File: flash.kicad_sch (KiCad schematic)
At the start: 0 parts

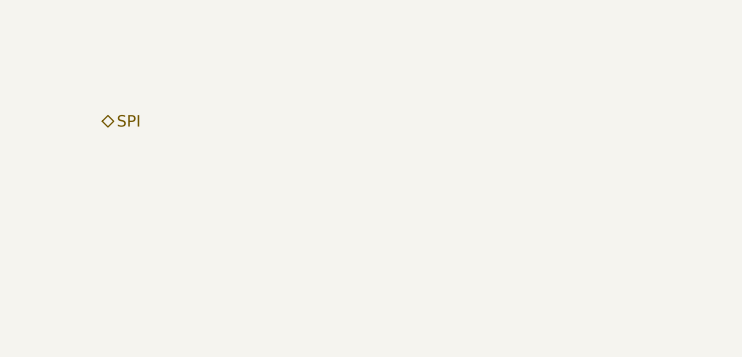
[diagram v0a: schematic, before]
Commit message: Added flash
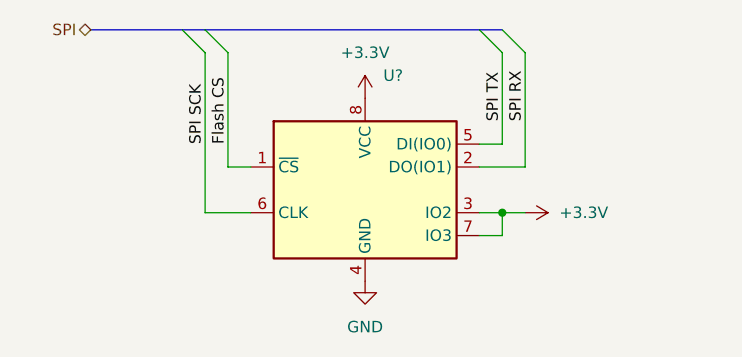
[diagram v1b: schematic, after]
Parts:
- added U?: ~, Package_SO:SOIC-8_5.23x5.23mm_P1.27mm, symbol Memory_Flash:W25Q32JVSS
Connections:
- new net +3V3: U?.3 (IO2), U?.7 (IO3), U?.8 (VCC)
- new net Flash CS: U?.1 (~{CS})
- new net GND: U?.4 (GND)
- new net SPI RX: U?.2 (DO(IO1))
- new net SPI SCK: U?.6 (CLK)
- new net SPI TX: U?.5 (DI(IO0))
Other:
- title: (none) -> Phoenix Flash
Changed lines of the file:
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@@
 (kicad_sch (version 20211123) (generator eeschema)
-  (paper "A4")
-  (hierarchical_label "SPI" (shape bidirectional) (at 25.4 31.75 0)
-    (effects (font (size 1.27 1.27)) (justify left))
+  (paper "A5")
+  (title_block
+    (title "Phoenix Flash")
+    (comment 1 "2022/10/19 WH")
+  )
+  (junction (at 69.85 41.91) (diameter 0) (color 0 0 0 0)
+  )
+  (bus_entry (at 36.83 21.59) (size 2.54 2.54)
+    (stroke (width 0) (type default) (color 0 0 0 0))
+  )
+  (bus_entry (at 34.29 21.59) (size 2.54 2.54)
+    (stroke (width 0) (type default) (color 0 0 0 0))
+  )
+  (bus_entry (at 67.31 21.59) (size 2.54 2.54)
+    (stroke (width 0) (type default) (color 0 0 0 0))
+  )
+  (bus_entry (at 69.85 21.59) (size 2.54 2.54)
+    (stroke (width 0) (type default) (color 0 0 0 0))
+  )
+  (bus (pts (xy 36.83 21.59) (xy 67.31 21.59))
+    (stroke (width 0) (type default) (color 0 0 0 0))
+  )
+  (wire (pts (xy 39.37 24.13) (xy 39.37 36.83))
+    (stroke (width 0) (type default) (color 0 0 0 0))
+  )
+  (wire (pts (xy 39.37 36.83) (xy 41.91 36.83))
+    (stroke (width 0) (type default) (color 0 0 0 0))
+  )
+  (wire (pts (xy 69.85 34.29) (xy 69.85 24.13))
+    (stroke (width 0) (type default) (color 0 0 0 0))
+  )
+  (wire (pts (xy 69.85 41.91) (xy 67.31 41.91))
+    (stroke (width 0) (type default) (color 0 0 0 0))
+  )
+  (wire (pts (xy 36.83 24.13) (xy 36.83 41.91))
+    (stroke (width 0) (type default) (color 0 0 0 0))
+  )
+  (bus (pts (xy 34.29 21.59) (xy 36.83 21.59))
+    (stroke (width 0) (type default) (color 0 0 0 0))
+  )
+  (wire (pts (xy 36.83 41.91) (xy 41.91 41.91))
+    (stroke (width 0) (type default) (color 0 0 0 0))
+  )
+  (bus (pts (xy 67.31 21.59) (xy 69.85 21.59))
+    (stroke (width 0) (type default) (color 0 0 0 0))
+  )
+  (wire (pts (xy 67.31 44.45) (xy 69.85 44.45))
+    (stroke (width 0) (type default) (color 0 0 0 0))
+  )
+  (wire (pts (xy 69.85 44.45) (xy 69.85 41.91))
+    (stroke (width 0) (type default) (color 0 0 0 0))
+  )
+  (wire (pts (xy 69.85 41.91) (xy 72.39 41.91))
+    (stroke (width 0) (type default) (color 0 0 0 0))
+  )
+  (wire (pts (xy 72.39 24.13) (xy 72.39 36.83))
+    (stroke (width 0) (type default) (color 0 0 0 0))
+  )
+  (wire (pts (xy 72.39 36.83) (xy 67.31 36.83))
+    (stroke (width 0) (type default) (color 0 0 0 0))
+  )
+  (wire (pts (xy 67.31 34.29) (xy 69.85 34.29))
+    (stroke (width 0) (type default) (color 0 0 0 0))
+  )
+  (bus (pts (xy 24.13 21.59) (xy 34.29 21.59))
+    (stroke (width 0) (type default) (color 0 0 0 0))
+  )
+  (label "SPI SCK" (at 36.83 34.29 90)
+    (effects (font (size 1.27 1.27)) (justify left bottom))
+  )
+  (label "SPI RX" (at 72.39 31.75 90)
+    (effects (font (size 1.27 1.27)) (justify left bottom))
+  )
+  (label "Flash CS" (at 39.37 34.29 90)
+    (effects (font (size 1.27 1.27)) (justify left bottom))
+  )
+  (label "SPI TX" (at 69.85 31.75 90)
+    (effects (font (size 1.27 1.27)) (justify left bottom))
+  )
+  (hierarchical_label "SPI" (shape bidirectional) (at 24.13 21.59 180)
+    (effects (font (size 1.27 1.27)) (justify right))
+  )
+  (symbol (lib_id "power:+3.3V") (at 72.39 41.91 270) (unit 1)
+    (in_bom yes) (on_board yes) (fields_autoplaced)
+    (property "Reference" "#PWR?" (id 0) (at 68.58 41.91 0)
+      (effects (font (size 1.27 1.27)) hide)
+    )
+    (property "Value" "+3.3V" (id 1) (at 76.2 41.9099 90)
+      (effects (font (size 1.27 1.27)) (justify left))
+    )
+    (property "Footprint" "" (id 2) (at 72.39 41.91 0)
+      (effects (font (size 1.27 1.27)) hide)
+    )
+    (property "Datasheet" "" (id 3) (at 72.39 41.91 0)
+      (effects (font (size 1.27 1.27)) hide)
+    )
+    (pin "1")
+  )
+  (symbol (lib_id "power:GND") (at 54.61 49.53 0) (unit 1)
+    (in_bom yes) (on_board yes) (fields_autoplaced)
+    (property "Reference" "#PWR?" (id 0) (at 54.61 55.88 0)
+      (effects (font (size 1.27 1.27)) hide)
+    )
+    (property "Value" "GND" (id 1) (at 54.61 54.61 0))
+    (property "Footprint" "" (id 2) (at 54.61 49.53 0)
+      (effects (font (size 1.27 1.27)) hide)
+    )
+    (property "Datasheet" "" (id 3) (at 54.61 49.53 0)
+      (effects (font (size 1.27 1.27)) hide)
+    )
+    (pin "1")
+  )
+  (symbol (lib_id "Memory_Flash:W25Q32JVSS") (at 54.61 39.37 0) (unit 1)
+    (in_bom yes) (on_board yes) (fields_autoplaced)
+    (property "Reference" "U?" (id 0) (at 56.6294 26.67 0)
+      (effects (font (size 1.27 1.27)) (justify left))
+    )
+    (property "Value" "~" (id 1) (at 56.6294 29.21 0)
+      (effects (font (size 1.27 1.27)) (justify left))
+    )
+    (property "Footprint" "Package_SO:SOIC-8_5.23x5.23mm_P1.27mm" (id 2) (at 54.61 39.37 0)
+      (effects (font (size 1.27 1.27)) hide)
+    )
+    (property "Datasheet" "http://www.winbond.com/resource-files/w25q32jv%20revg%2003272018%20plus.pdf" (id 3) (at 54.61 39.37 0)
+      (effects (font (size 1.27 1.27)) hide)
+    )
+    (property "JLC" "SOP-8_5.2x5.3x1.27P" (id 4) (at 54.61 39.37 0)
+      (effects (font (size 1.27 1.27)) hide)
+    )
+    (property "LCSC" "C83140" (id 5) (at 54.61 39.37 0)
+      (effects (font (size 1.27 1.27)) hide)
+    )
+    (pin "1")
+    (pin "2")
+    (pin "3")
+    (pin "4")
+    (pin "5")
+    (pin "6")
+    (pin "7")
+    (pin "8")
+  )
+  (symbol (lib_id "power:+3.3V") (at 54.61 29.21 0) (unit 1)
+    (in_bom yes) (on_board yes) (fields_autoplaced)
+    (property "Reference" "#PWR?" (id 0) (at 54.61 33.02 0)
+      (effects (font (size 1.27 1.27)) hide)
+    )
+    (property "Value" "+3.3V" (id 1) (at 54.61 24.13 0))
+    (property "Footprint" "" (id 2) (at 54.61 29.21 0)
+      (effects (font (size 1.27 1.27)) hide)
+    )
+    (property "Datasheet" "" (id 3) (at 54.61 29.21 0)
+      (effects (font (size 1.27 1.27)) hide)
+    )
+    (pin "1")
   )
 )

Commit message: Added decoupling cap to flash
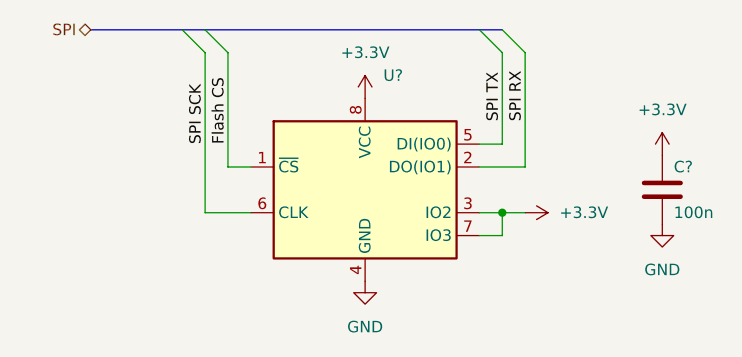
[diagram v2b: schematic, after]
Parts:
- added C?: 100n, Capacitor_SMD:C_0603_1608Metric, symbol Device:C
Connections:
- net +3V3: now also C?.1
- net GND: now also C?.2
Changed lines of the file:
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@@
     (pin "1")
+  )
+  (symbol (lib_id "power:+3.3V") (at 87.63 35.56 0) (unit 1)
+    (in_bom yes) (on_board yes) (fields_autoplaced)
+    (property "Reference" "#PWR?" (id 0) (at 87.63 39.37 0)
+      (effects (font (size 1.27 1.27)) hide)
+    )
+    (property "Value" "+3.3V" (id 1) (at 87.63 30.48 0))
+    (property "Footprint" "" (id 2) (at 87.63 35.56 0)
+      (effects (font (size 1.27 1.27)) hide)
+    )
+    (property "Datasheet" "" (id 3) (at 87.63 35.56 0)
+      (effects (font (size 1.27 1.27)) hide)
+    )
+    (pin "1")
+  )
+  (symbol (lib_id "Device:C") (at 87.63 39.37 0) (unit 1)
+    (in_bom yes) (on_board yes)
+    (property "Reference" "C?" (id 0) (at 88.9 36.83 0)
+      (effects (font (size 1.27 1.27)) (justify left))
+    )
+    (property "Value" "100n" (id 1) (at 88.9 41.91 0)
+      (effects (font (size 1.27 1.27)) (justify left))
+    )
+    (property "Footprint" "Capacitor_SMD:C_0603_1608Metric" (id 2) (at 88.5952 43.18 0)
+      (effects (font (size 1.27 1.27)) hide)
+    )
+    (property "Datasheet" "~" (id 3) (at 87.63 39.37 0)
+      (effects (font (size 1.27 1.27)) hide)
+    )
+    (property "LCSC" "C14663" (id 4) (at 87.63 39.37 0)
+      (effects (font (size 1.27 1.27)) hide)
+    )
+    (property "JLC" "0603" (id 5) (at 87.63 39.37 0)
+      (effects (font (size 1.27 1.27)) hide)
+    )
+    (pin "1")
+    (pin "2")
   )
   (symbol (lib_id "Memory_Flash:W25Q32JVSS") (at 54.61 39.37 0) (unit 1)
@@
     (pin "8")
   )
+  (symbol (lib_id "power:GND") (at 87.63 43.18 0) (unit 1)
+    (in_bom yes) (on_board yes) (fields_autoplaced)
+    (property "Reference" "#PWR?" (id 0) (at 87.63 49.53 0)
+      (effects (font (size 1.27 1.27)) hide)
+    )
+    (property "Value" "GND" (id 1) (at 87.63 48.26 0))
+    (property "Footprint" "" (id 2) (at 87.63 43.18 0)
+      (effects (font (size 1.27 1.27)) hide)
+    )
+    (property "Datasheet" "" (id 3) (at 87.63 43.18 0)
+      (effects (font (size 1.27 1.27)) hide)
+    )
+    (pin "1")
+  )
   (symbol (lib_id "power:+3.3V") (at 54.61 29.21 0) (unit 1)

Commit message: Fixed bus names
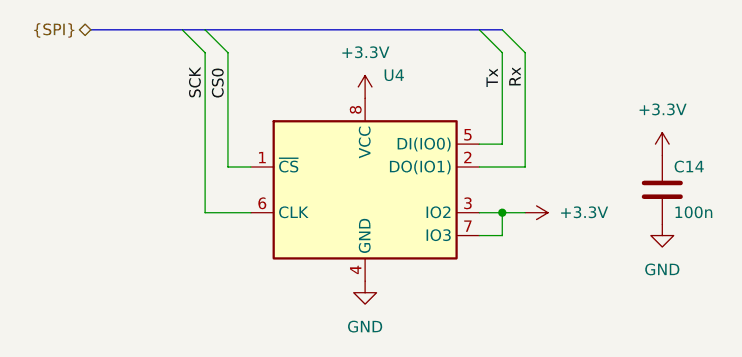
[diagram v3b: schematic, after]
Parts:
- gave numbers to parts that had none: 2
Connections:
- net Flash CS renamed CS0
- net SPI RX renamed Rx
- net SPI SCK renamed SCK
- net SPI TX renamed Tx
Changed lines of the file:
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@@
     (stroke (width 0) (type default) (color 0 0 0 0))
   )
-  (label "SPI SCK" (at 36.83 34.29 90)
+  (label "SCK" (at 36.83 29.21 90)
     (effects (font (size 1.27 1.27)) (justify left bottom))
   )
-  (label "SPI RX" (at 72.39 31.75 90)
+  (label "Rx" (at 72.39 27.94 90)
     (effects (font (size 1.27 1.27)) (justify left bottom))
   )
-  (label "Flash CS" (at 39.37 34.29 90)
+  (label "CS0" (at 39.37 29.21 90)
     (effects (font (size 1.27 1.27)) (justify left bottom))
   )
-  (label "SPI TX" (at 69.85 31.75 90)
+  (label "Tx" (at 69.85 27.94 90)
     (effects (font (size 1.27 1.27)) (justify left bottom))
   )
-  (hierarchical_label "SPI" (shape bidirectional) (at 24.13 21.59 180)
+  (hierarchical_label "{SPI}" (shape bidirectional) (at 24.13 21.59 180)
     (effects (font (size 1.27 1.27)) (justify right))
   )
   (symbol (lib_id "power:+3.3V") (at 72.39 41.91 270) (unit 1)
     (in_bom yes) (on_board yes) (fields_autoplaced)
-    (property "Reference" "#PWR?" (id 0) (at 68.58 41.91 0)
+    (property "Reference" "#PWR0130" (id 0) (at 68.58 41.91 0)
       (effects (font (size 1.27 1.27)) hide)
     )
@@
   (symbol (lib_id "power:GND") (at 54.61 49.53 0) (unit 1)
     (in_bom yes) (on_board yes) (fields_autoplaced)
-    (property "Reference" "#PWR?" (id 0) (at 54.61 55.88 0)
+    (property "Reference" "#PWR0129" (id 0) (at 54.61 55.88 0)
       (effects (font (size 1.27 1.27)) hide)
     )
@@
   (symbol (lib_id "power:+3.3V") (at 87.63 35.56 0) (unit 1)
     (in_bom yes) (on_board yes) (fields_autoplaced)
-    (property "Reference" "#PWR?" (id 0) (at 87.63 39.37 0)
+    (property "Reference" "#PWR0131" (id 0) (at 87.63 39.37 0)
       (effects (font (size 1.27 1.27)) hide)
     )
@@
   (symbol (lib_id "Device:C") (at 87.63 39.37 0) (unit 1)
     (in_bom yes) (on_board yes)
-    (property "Reference" "C?" (id 0) (at 88.9 36.83 0)
+    (property "Reference" "C14" (id 0) (at 88.9 36.83 0)
       (effects (font (size 1.27 1.27)) (justify left))
     )
@@
   (symbol (lib_id "Memory_Flash:W25Q32JVSS") (at 54.61 39.37 0) (unit 1)
     (in_bom yes) (on_board yes) (fields_autoplaced)
-    (property "Reference" "U?" (id 0) (at 56.6294 26.67 0)
+    (property "Reference" "U4" (id 0) (at 56.6294 26.67 0)
       (effects (font (size 1.27 1.27)) (justify left))
     )
@@
   (symbol (lib_id "power:GND") (at 87.63 43.18 0) (unit 1)
     (in_bom yes) (on_board yes) (fields_autoplaced)
-    (property "Reference" "#PWR?" (id 0) (at 87.63 49.53 0)
+    (property "Reference" "#PWR0133" (id 0) (at 87.63 49.53 0)
       (effects (font (size 1.27 1.27)) hide)
     )
@@
   (symbol (lib_id "power:+3.3V") (at 54.61 29.21 0) (unit 1)
     (in_bom yes) (on_board yes) (fields_autoplaced)
-    (property "Reference" "#PWR?" (id 0) (at 54.61 33.02 0)
+    (property "Reference" "#PWR0128" (id 0) (at 54.61 33.02 0)
       (effects (font (size 1.27 1.27)) hide)
     )

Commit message: Various updates because I forgot to commit for a while
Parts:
- renumbered C14 to C19, U4 to U7
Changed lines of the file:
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@@
   (symbol (lib_id "power:+3.3V") (at 72.39 41.91 270) (unit 1)
     (in_bom yes) (on_board yes) (fields_autoplaced)
-    (property "Reference" "#PWR0130" (id 0) (at 68.58 41.91 0)
+    (property "Reference" "#PWR040" (id 0) (at 68.58 41.91 0)
       (effects (font (size 1.27 1.27)) hide)
     )
@@
   (symbol (lib_id "power:GND") (at 54.61 49.53 0) (unit 1)
     (in_bom yes) (on_board yes) (fields_autoplaced)
-    (property "Reference" "#PWR0129" (id 0) (at 54.61 55.88 0)
+    (property "Reference" "#PWR039" (id 0) (at 54.61 55.88 0)
       (effects (font (size 1.27 1.27)) hide)
     )
@@
   (symbol (lib_id "power:+3.3V") (at 87.63 35.56 0) (unit 1)
     (in_bom yes) (on_board yes) (fields_autoplaced)
-    (property "Reference" "#PWR0131" (id 0) (at 87.63 39.37 0)
+    (property "Reference" "#PWR041" (id 0) (at 87.63 39.37 0)
       (effects (font (size 1.27 1.27)) hide)
     )
@@
   (symbol (lib_id "Device:C") (at 87.63 39.37 0) (unit 1)
     (in_bom yes) (on_board yes)
-    (property "Reference" "C14" (id 0) (at 88.9 36.83 0)
+    (property "Reference" "C19" (id 0) (at 88.9 36.83 0)
       (effects (font (size 1.27 1.27)) (justify left))
     )
@@
   (symbol (lib_id "Memory_Flash:W25Q32JVSS") (at 54.61 39.37 0) (unit 1)
     (in_bom yes) (on_board yes) (fields_autoplaced)
-    (property "Reference" "U4" (id 0) (at 56.6294 26.67 0)
+    (property "Reference" "U7" (id 0) (at 56.6294 26.67 0)
       (effects (font (size 1.27 1.27)) (justify left))
     )
@@
   (symbol (lib_id "power:GND") (at 87.63 43.18 0) (unit 1)
     (in_bom yes) (on_board yes) (fields_autoplaced)
-    (property "Reference" "#PWR0133" (id 0) (at 87.63 49.53 0)
+    (property "Reference" "#PWR042" (id 0) (at 87.63 49.53 0)
       (effects (font (size 1.27 1.27)) hide)
     )
@@
   (symbol (lib_id "power:+3.3V") (at 54.61 29.21 0) (unit 1)
     (in_bom yes) (on_board yes) (fields_autoplaced)
-    (property "Reference" "#PWR0128" (id 0) (at 54.61 33.02 0)
+    (property "Reference" "#PWR038" (id 0) (at 54.61 33.02 0)
       (effects (font (size 1.27 1.27)) hide)
     )

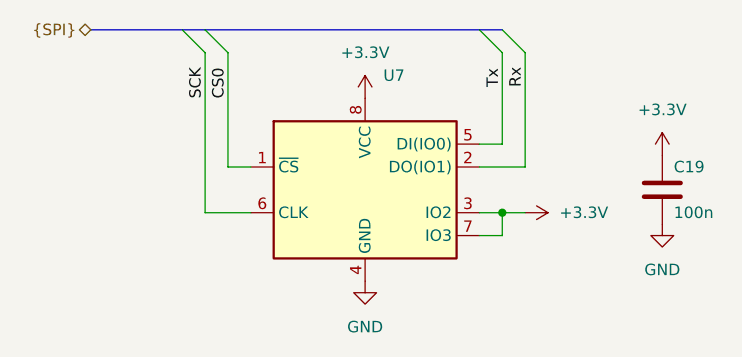
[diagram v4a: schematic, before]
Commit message: Connected the sensors, flash chip, Need to connect the radio and GPS
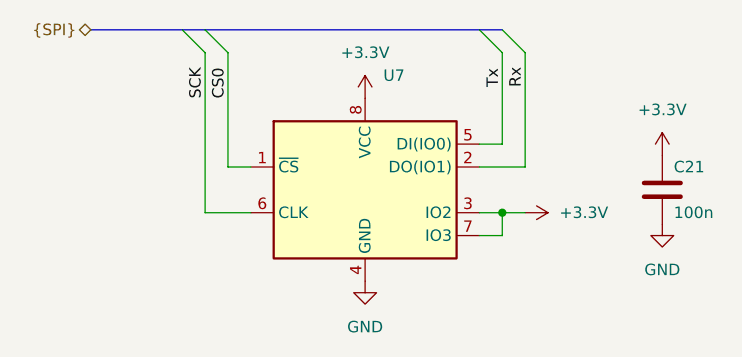
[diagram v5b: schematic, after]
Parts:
- renumbered C19 to C21
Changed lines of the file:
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@@
   (symbol (lib_id "power:+3.3V") (at 72.39 41.91 270) (unit 1)
     (in_bom yes) (on_board yes) (fields_autoplaced)
-    (property "Reference" "#PWR040" (id 0) (at 68.58 41.91 0)
+    (property "Reference" "#PWR042" (id 0) (at 68.58 41.91 0)
       (effects (font (size 1.27 1.27)) hide)
     )
@@
   (symbol (lib_id "power:GND") (at 54.61 49.53 0) (unit 1)
     (in_bom yes) (on_board yes) (fields_autoplaced)
-    (property "Reference" "#PWR039" (id 0) (at 54.61 55.88 0)
+    (property "Reference" "#PWR041" (id 0) (at 54.61 55.88 0)
       (effects (font (size 1.27 1.27)) hide)
     )
@@
   (symbol (lib_id "power:+3.3V") (at 87.63 35.56 0) (unit 1)
     (in_bom yes) (on_board yes) (fields_autoplaced)
-    (property "Reference" "#PWR041" (id 0) (at 87.63 39.37 0)
+    (property "Reference" "#PWR043" (id 0) (at 87.63 39.37 0)
       (effects (font (size 1.27 1.27)) hide)
     )
@@
   (symbol (lib_id "Device:C") (at 87.63 39.37 0) (unit 1)
     (in_bom yes) (on_board yes)
-    (property "Reference" "C19" (id 0) (at 88.9 36.83 0)
+    (property "Reference" "C21" (id 0) (at 88.9 36.83 0)
       (effects (font (size 1.27 1.27)) (justify left))
     )
@@
   (symbol (lib_id "power:GND") (at 87.63 43.18 0) (unit 1)
     (in_bom yes) (on_board yes) (fields_autoplaced)
-    (property "Reference" "#PWR042" (id 0) (at 87.63 49.53 0)
+    (property "Reference" "#PWR044" (id 0) (at 87.63 49.53 0)
       (effects (font (size 1.27 1.27)) hide)
     )
@@
   (symbol (lib_id "power:+3.3V") (at 54.61 29.21 0) (unit 1)
     (in_bom yes) (on_board yes) (fields_autoplaced)
-    (property "Reference" "#PWR038" (id 0) (at 54.61 33.02 0)
+    (property "Reference" "#PWR040" (id 0) (at 54.61 33.02 0)
       (effects (font (size 1.27 1.27)) hide)
     )

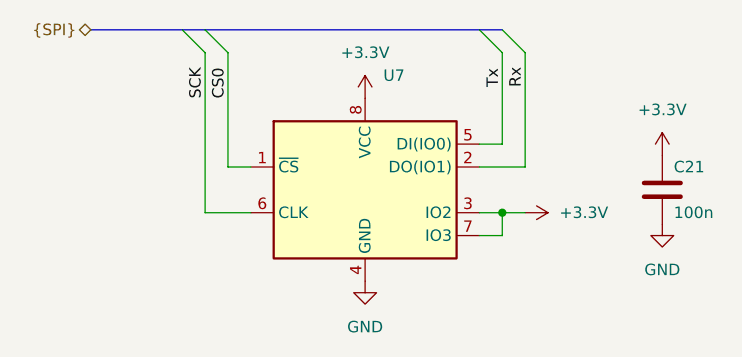
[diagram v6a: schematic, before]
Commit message: Added polyfuse
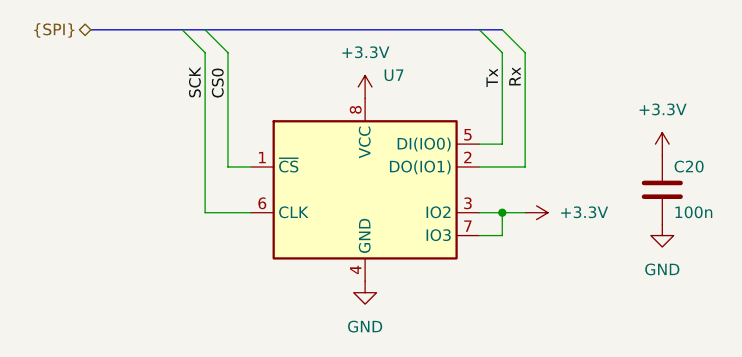
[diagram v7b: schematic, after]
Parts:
- renumbered C21 to C20
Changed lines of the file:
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@@
   (symbol (lib_id "power:+3.3V") (at 72.39 41.91 270) (unit 1)
     (in_bom yes) (on_board yes) (fields_autoplaced)
-    (property "Reference" "#PWR042" (id 0) (at 68.58 41.91 0)
+    (property "Reference" "#PWR040" (id 0) (at 68.58 41.91 0)
       (effects (font (size 1.27 1.27)) hide)
     )
@@
   (symbol (lib_id "power:GND") (at 54.61 49.53 0) (unit 1)
     (in_bom yes) (on_board yes) (fields_autoplaced)
-    (property "Reference" "#PWR041" (id 0) (at 54.61 55.88 0)
+    (property "Reference" "#PWR039" (id 0) (at 54.61 55.88 0)
       (effects (font (size 1.27 1.27)) hide)
     )
@@
   (symbol (lib_id "power:+3.3V") (at 87.63 35.56 0) (unit 1)
     (in_bom yes) (on_board yes) (fields_autoplaced)
-    (property "Reference" "#PWR043" (id 0) (at 87.63 39.37 0)
+    (property "Reference" "#PWR041" (id 0) (at 87.63 39.37 0)
       (effects (font (size 1.27 1.27)) hide)
     )
@@
   (symbol (lib_id "Device:C") (at 87.63 39.37 0) (unit 1)
     (in_bom yes) (on_board yes)
-    (property "Reference" "C21" (id 0) (at 88.9 36.83 0)
+    (property "Reference" "C20" (id 0) (at 88.9 36.83 0)
       (effects (font (size 1.27 1.27)) (justify left))
     )
@@
   (symbol (lib_id "power:GND") (at 87.63 43.18 0) (unit 1)
     (in_bom yes) (on_board yes) (fields_autoplaced)
-    (property "Reference" "#PWR044" (id 0) (at 87.63 49.53 0)
+    (property "Reference" "#PWR042" (id 0) (at 87.63 49.53 0)
       (effects (font (size 1.27 1.27)) hide)
     )
@@
   (symbol (lib_id "power:+3.3V") (at 54.61 29.21 0) (unit 1)
     (in_bom yes) (on_board yes) (fields_autoplaced)
-    (property "Reference" "#PWR040" (id 0) (at 54.61 33.02 0)
+    (property "Reference" "#PWR038" (id 0) (at 54.61 33.02 0)
       (effects (font (size 1.27 1.27)) hide)
     )
